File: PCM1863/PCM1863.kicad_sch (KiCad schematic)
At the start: 78 parts, among them IC1 SN74AUC1G126DCKR, IC2 NCP163ASN330T1G, IC3 NCP163ASN330T1G, IC4 TXB0101DBVT, J1 Conn_01x10_Male, J2 Conn_01x10_Male, J3 Conn_01x10_Male, J4 USB_B_Micro, U1 PCM1863, Y1 ASE-24.000MHZ-ET, Y2 ASE-22.000MHZ-ET

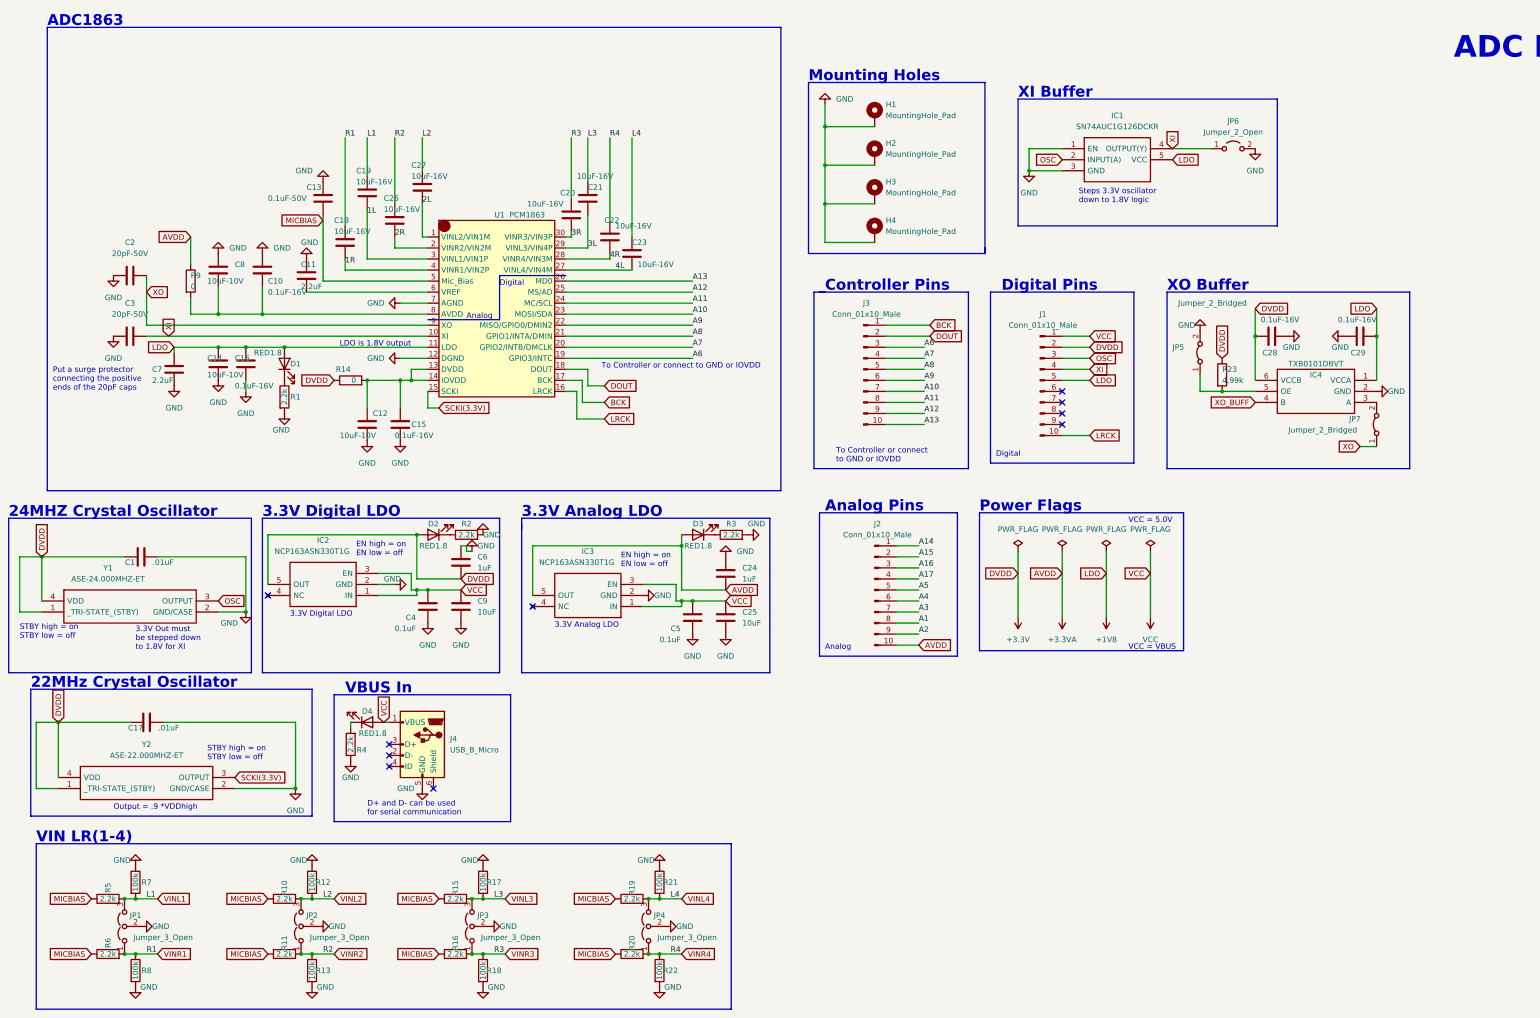
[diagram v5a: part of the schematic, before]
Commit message: schematic updates for ADC
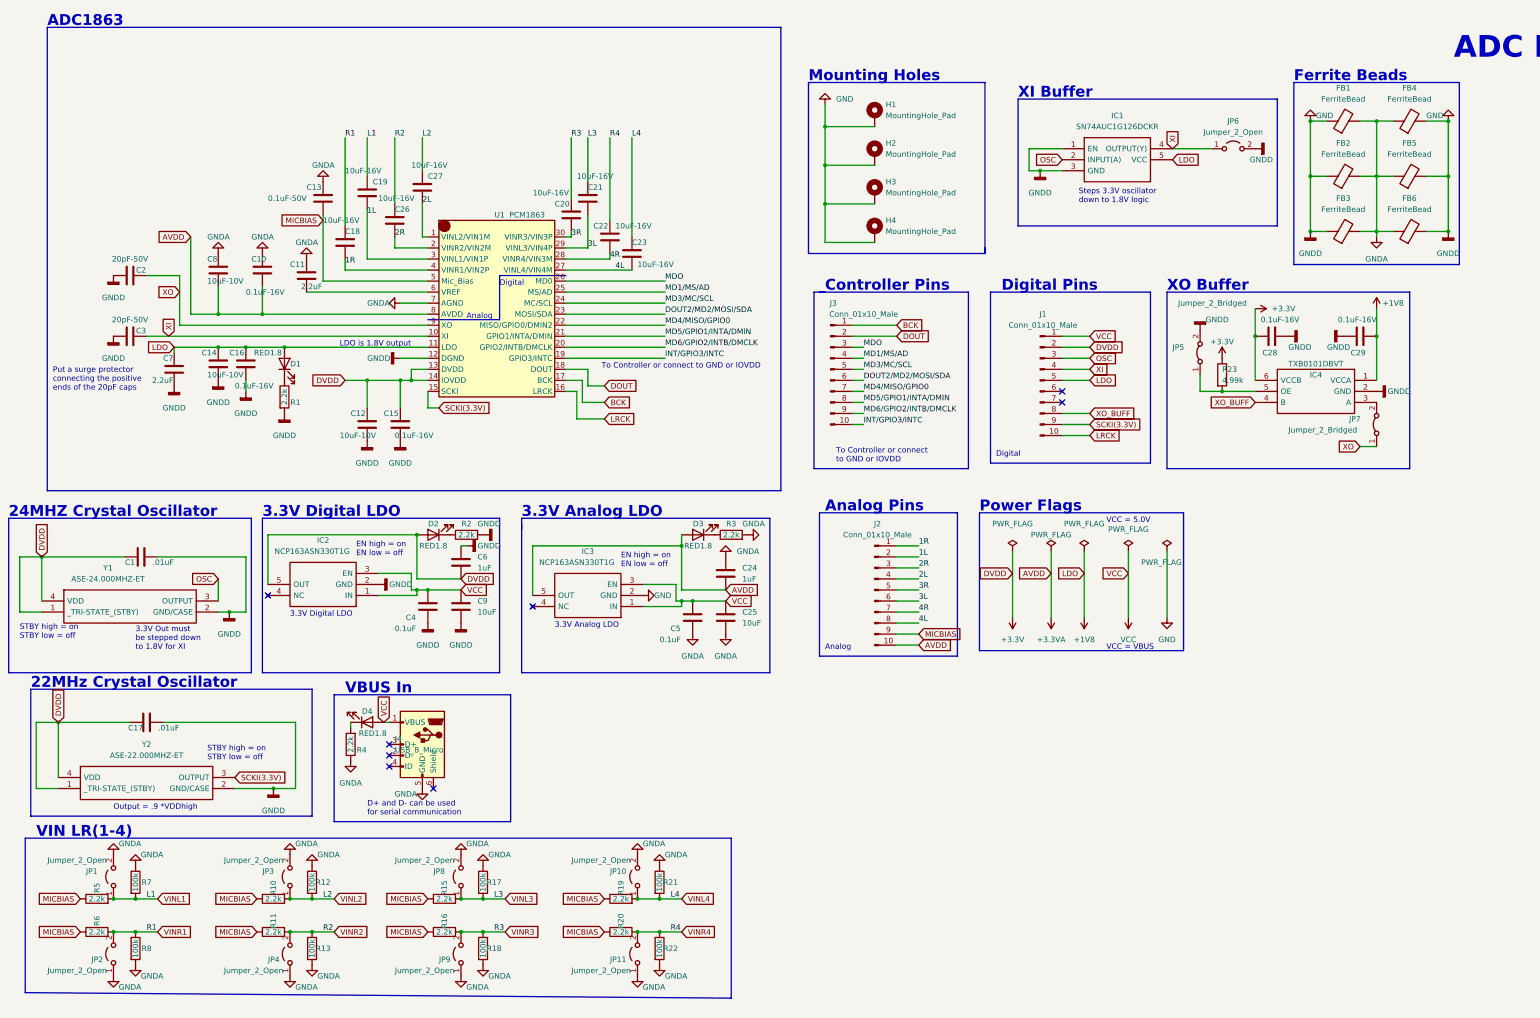
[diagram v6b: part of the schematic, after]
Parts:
- removed JP1, JP2, JP3, JP4: Jumper_3_Open, symbol Jumper:Jumper_3_Open
- removed R14, R9: 0, Resistor_SMD:R_0603_1608Metric_Pad0.98x0.95mm_HandSolder, symbol Device:R
- added FB1, FB2, FB3, FB4, FB5, FB6: FerriteBead, Inductor_SMD:L_0603_1608Metric_Pad1.05x0.95mm_HandSolder, symbol Device:FerriteBead
- added JP1, JP10, JP11, JP2, JP3, JP4, JP8, JP9: Jumper_2_Open, custom_lib:TestPoint_Bridge_Pitch2.54mm_Drill0.7mm, symbol Jumper:Jumper_2_Open
- C10, C15, C16, C28, C29: footprint Capacitor_SMD:C_0402_1005Metric_Pad0.74x0.62mm_HandSolder -> Capacitor_SMD:C_0603_1608Metric_Pad1.08x0.95mm_HandSolder
- C18, C19, C20, C21, C22, C23, C26, C27, C8: footprint Capacitor_SMD:C_0805_2012Metric_Pad1.18x1.45mm_HandSolder -> Capacitor_SMD:C_0603_1608Metric_Pad1.08x0.95mm_HandSolder
- JP5, JP6, JP7: footprint TestPoint:TestPoint_Bridge_Pitch2.54mm_Drill1.0mm -> custom_lib:TestPoint_Bridge_Pitch2.54mm_Drill0.7mm
- R12, R13, R17, R18, R21, R22, R23, R7, R8: footprint Resistor_SMD:R_0402_1005Metric_Pad0.72x0.64mm_HandSolder -> Resistor_SMD:R_0603_1608Metric_Pad0.98x0.95mm_HandSolder
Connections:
- net A1 is gone; now on net 4L: J2.8 (Pin_8)
- net A14 is gone; now on net 1R: J2.1 (Pin_1)
- net A15 is gone; now on net 1L: J2.2 (Pin_2)
- net A16 is gone; now on net 2R: J2.3 (Pin_3)
- net A17 is gone; now on net 2L: J2.4 (Pin_4)
- net A2 is gone; now on net MICBIAS: J2.9 (Pin_9)
- net A3 is gone; now on net 4R: J2.7 (Pin_7)
- net A4 is gone; now on net 3L: J2.6 (Pin_6)
- net A5 is gone; now on net 3R: J2.5 (Pin_5)
- net +3.3VA: now also C10.2, C8.2, U1.8 (AVDD)
- net +3V3: now also C12.1, C15.1, U1.13 (DVDD), U1.14 (IOVDD)
- net GND: now also FB1.1, FB2.1, FB3.1, FB4.2, FB5.2, FB6.2; no longer C10.1, C11.1, C13.1, C24.1, C25.2, C5.2, C8.1, J4.5 (GND), R12.1, R13.2, R17.1, R18.2, R21.1, R22.2, R3.2, R4.1, R7.1, R8.2, U1.7 (AGND)
- net SCKI(3.3V): now also J1.9 (Pin_9)
- net VINL1: now also JP1.1 (A)
- net VINL2: now also JP3.1 (A)
- net VINL3: now also JP8.1 (A)
- net VINL4: now also JP10.1 (A)
- net VINR1: now also JP2.2 (B)
- net VINR2: now also JP4.2 (B)
- net VINR3: now also JP9.2 (B)
- net VINR4: now also JP11.2 (B)
- net XO_BUFF: now also J1.8 (Pin_8)
- net A10 renamed DOUT2/MD2/MOSI/SDA
- net DOUT2/MD2/MOSI/SDA: now also J3.6 (Pin_6); no longer J3.7 (Pin_7)
- net A11 renamed MD3/MC/SCL
- net MD3/MC/SCL: now also J3.5 (Pin_5); no longer J3.8 (Pin_8)
- net A12 renamed MD1/MS/AD
- net MD1/MS/AD: now also J3.4 (Pin_4); no longer J3.9 (Pin_9)
- net A13 renamed INT/GPIO3/INTC
- net INT/GPIO3/INTC: now also U1.19 (GPIO3/INTC); no longer U1.26 (MD0)
- net A6 renamed MDO
- net MDO: now also U1.26 (MD0); no longer U1.19 (GPIO3/INTC)
- net A7 renamed MD6/GPIO2/INTB/DMCLK
- net MD6/GPIO2/INTB/DMCLK: now also J3.9 (Pin_9); no longer J3.4 (Pin_4)
- net A8 renamed MD5/GPIO1/INTA/DMIN
- net MD5/GPIO1/INTA/DMIN: now also J3.8 (Pin_8); no longer J3.5 (Pin_5)
- net A9 renamed MD4/MISO/GPIO0
- net MD4/MISO/GPIO0: now also J3.7 (Pin_7); no longer J3.6 (Pin_6)
- new net GNDA: C10.1, C11.1, C13.1, C24.1, C25.2, C5.2, C8.1, FB1.2, FB2.2, FB3.2, FB4.1, FB5.1, FB6.1, J4.5 (GND), JP1.2 (B), JP10.2 (B), JP11.1 (A), JP2.1 (A), JP3.2 (B), JP4.1 (A), JP8.2 (B), JP9.1 (A), R12.1, R13.2, R17.1, R18.2, R21.1, R22.2, R3.2, R4.1, R7.1, R8.2, U1.7 (AGND)
- no-connect marks 10 -> 8
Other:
- note added: "Ferrite Beads"
- moved on the sheet: J3, R10, R11, R13, R15, R16, R18, R19, R20, R22, R5, R6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

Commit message: pcb grouping
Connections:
- net GND: no longer IC3.2 (GND)
- net GNDA: now also IC3.2 (GND)
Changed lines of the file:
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@@
-    (pin "1")
-  )
-  (symbol (lib_id "power:GND") (at 157.48 146.05 90) (unit 1)
-    (in_bom yes) (on_board yes)
-    (property "Reference" "#PWR0126" (id 0) (at 163.83 146.05 0)
-      (effects (font (size 1.27 1.27)) hide)
-    )
-    (property "Value" "GND" (id 1) (at 160.02 146.05 90)
-      (effects (font (size 1.27 1.27)) (justify right))
-    )
-    (property "Footprint" "" (id 2) (at 157.48 146.05 0)
-      (effects (font (size 1.27 1.27)) hide)
-    )
-    (property "Datasheet" "" (id 3) (at 157.48 146.05 0)
-      (effects (font (size 1.27 1.27)) hide)
-    )
     (pin "1")
   )
@@
     (pin "1")
   )
+  (symbol (lib_id "power:GNDA") (at 157.48 146.05 90) (unit 1)
+    (in_bom yes) (on_board yes)
+    (property "Reference" "#PWR?" (id 0) (at 163.83 146.05 0)
+      (effects (font (size 1.27 1.27)) hide)
+    )
+    (property "Value" "GNDA" (id 1) (at 160.02 144.78 90)
+      (effects (font (size 1.27 1.27)) (justify right))
+    )
+    (property "Footprint" "" (id 2) (at 157.48 146.05 0)
+      (effects (font (size 1.27 1.27)) hide)
+    )
+    (property "Datasheet" "" (id 3) (at 157.48 146.05 0)
+      (effects (font (size 1.27 1.27)) hide)
+    )
+    (pin "1")
+  )
   (symbol (lib_id "Device:R") (at 152.4 223.52 90) (unit 1)
     (in_bom yes) (on_board yes)
@@
       (reference "#PWR0125") (unit 1) (value "GNDA") (footprint "")
     )
-    (path "/96ae2e58-59ff-4772-87a2-8a0e4efc4221"
-      (reference "#PWR0126") (unit 1) (value "GND") (footprint "")
-    )
     (path "/8206264a-b333-4f9c-be7b-7fda8663f2d7"
       (reference "#PWR0127") (unit 1) (value "GNDA") (footprint "")
@@
       (reference "#PWR0159") (unit 1) (value "GND") (footprint "")
     )
+    (path "/e4a5f715-9288-4509-8816-3f5752571dcd"
+      (reference "#PWR?") (unit 1) (value "GNDA") (footprint "")
+    )
     (path "/0c2dffd9-4bf4-46de-b591-2fa76c6eabf3"
